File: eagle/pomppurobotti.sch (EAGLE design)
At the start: 23 parts, among them Q1 MOSFET-NCHANNELFQP30N06L

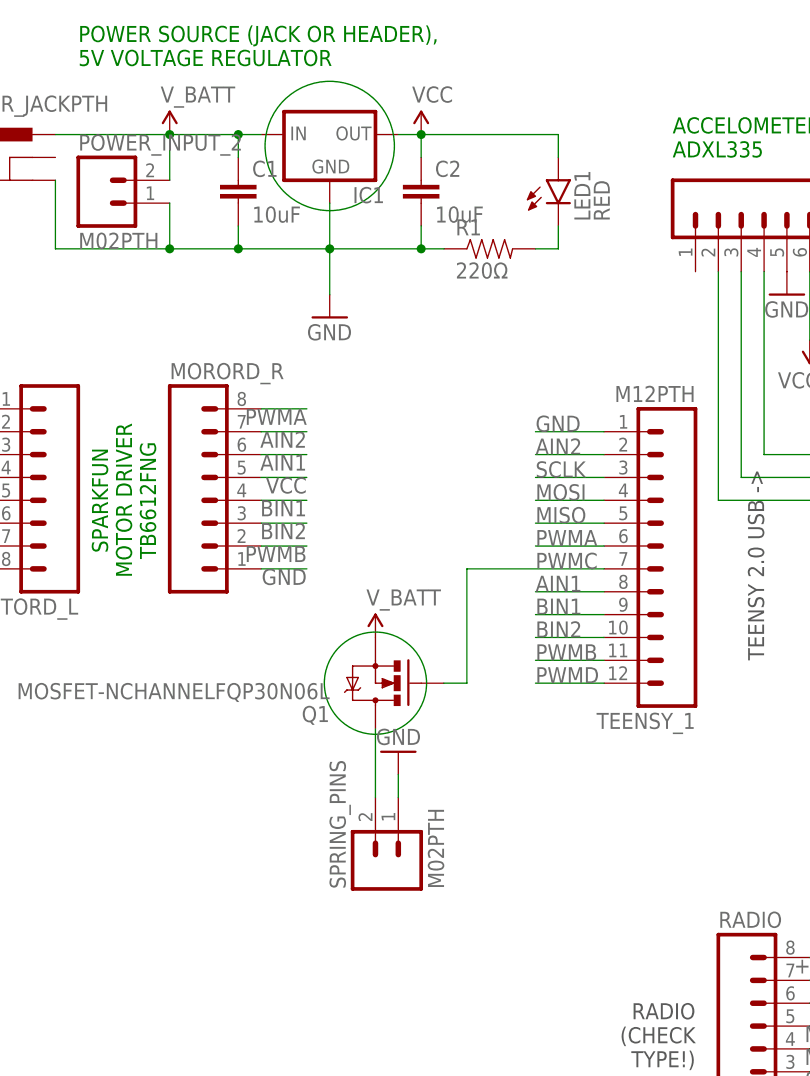
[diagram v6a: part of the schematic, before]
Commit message: Add Arduino tests and modified RF library. Update Eagle schematics.
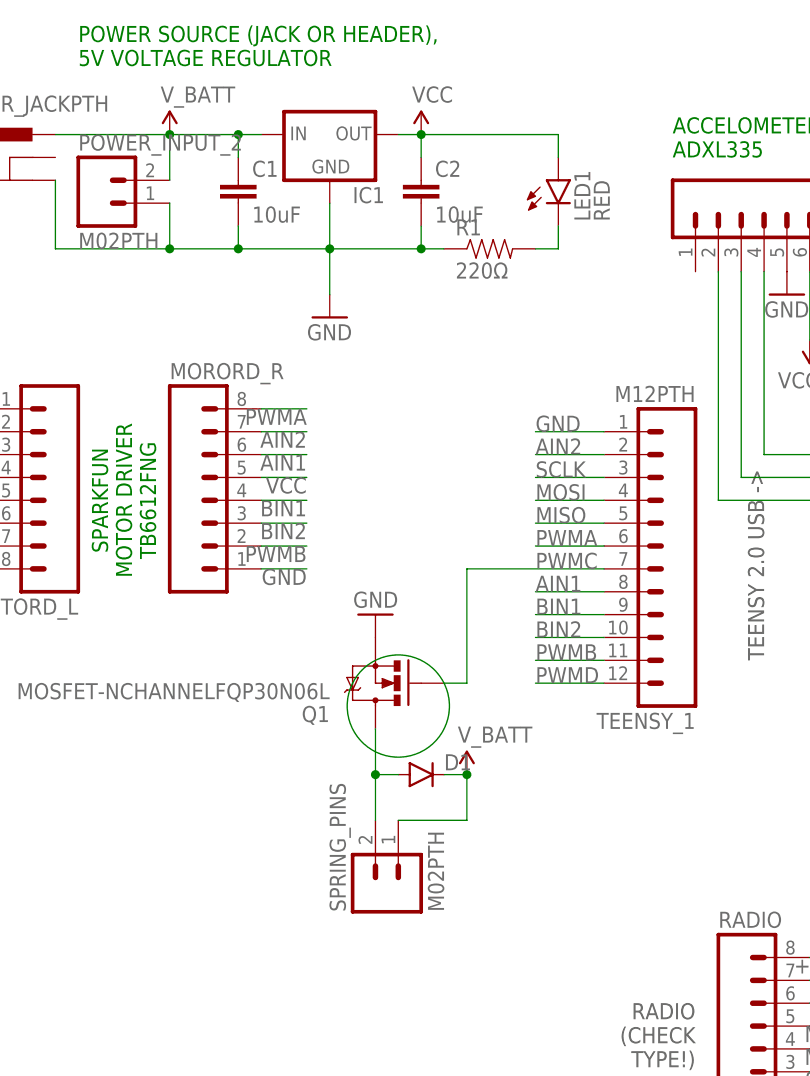
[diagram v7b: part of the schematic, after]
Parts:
- added D1: (no value), SparkFun-DiscreteSemi:DIODEPTH
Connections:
- net GND: now also Q1.S; no longer SPRING_PINS.1
- net N$5: now also D1.A
- net V_BATT: now also D1.C, SPRING_PINS.1; no longer Q1.S
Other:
- moved on the sheet: SPRING_PINS
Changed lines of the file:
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@@
 <layers>
 <layer number="1" name="Top" color="4" fill="1" visible="no" active="no"/>
-<layer number="16" name="Bottom" color="1" fill="1" visible="no" active="no"/>
+<layer number="16" name="Bottom" color="9" fill="1" visible="no" active="no"/>
 <layer number="17" name="Pads" color="2" fill="1" visible="no" active="no"/>
 <layer number="18" name="Vias" color="2" fill="1" visible="no" active="no"/>
@@
 <part name="SUPPLY4" library="SparkFun-Aesthetics" deviceset="V_BATT" device=""/>
 <part name="SUPPLY10" library="SparkFun-Aesthetics" deviceset="V_BATT" device=""/>
+<part name="D1" library="SparkFun-DiscreteSemi" deviceset="DIODE" device="PTH"/>
 </parts>
 <sheets>
@@
 <text x="238.76" y="5.08" size="1.778" layer="91">EXTRA
 PINS</text>
-<circle x="127" y="-5.08" radius="5.6796125" width="0.1524" layer="91"/>
-<circle x="121.92" y="54.61" radius="7.184203125" width="0.1524" layer="91"/>
+<circle x="129.54" y="-7.62" radius="5.6796125" width="0.1524" layer="91"/>
 </plain>
 <instances>
@@
 <instance part="LED2" gate="G$1" x="195.58" y="-17.78"/>
 <instance part="GND2" gate="1" x="195.58" y="-25.4"/>
-<instance part="SPRING_PINS" gate="G$1" x="129.54" y="-25.4" rot="R90"/>
-<instance part="GND3" gate="1" x="129.54" y="-12.7" rot="R180"/>
+<instance part="SPRING_PINS" gate="G$1" x="129.54" y="-27.94" rot="R90"/>
+<instance part="GND3" gate="1" x="127" y="2.54" rot="R180"/>
 <instance part="S1" gate="G$1" x="205.74" y="-2.54" smashed="yes">
 <attribute name="NAME" x="203.2" y="-5.08" size="1.778" layer="95"/>
@@
 <instance part="POWER_INPUT_2" gate="G$1" x="96.52" y="48.26"/>
 <instance part="SUPPLY9" gate="G$1" x="104.14" y="55.88"/>
-<instance part="SUPPLY4" gate="G$1" x="127" y="0"/>
+<instance part="SUPPLY4" gate="G$1" x="137.16" y="-15.24"/>
 <instance part="SUPPLY10" gate="G$1" x="83.82" y="25.4" rot="R90"/>
+<instance part="D1" gate="G$1" x="132.08" y="-15.24"/>
 </instances>
 <busses>
@@
 </segment>
 <segment>
-<pinref part="SPRING_PINS" gate="G$1" pin="1"/>
-<pinref part="GND3" gate="1" pin="GND"/>
-<wire x1="129.54" y1="-17.78" x2="129.54" y2="-15.24" width="0.1524" layer="91"/>
-</segment>
-<segment>
 <pinref part="ACCELOM" gate="G$1" pin="5"/>
 <pinref part="GND4" gate="1" pin="GND"/>
@@
 <pinref part="GND8" gate="1" pin="GND"/>
 <pinref part="RV1" gate="G$1" pin="E"/>
+</segment>
+<segment>
+<pinref part="Q1" gate="G$1" pin="S"/>
+<pinref part="GND3" gate="1" pin="GND"/>
 </segment>
 </net>
@@
 <pinref part="Q1" gate="G$1" pin="D"/>
 <pinref part="SPRING_PINS" gate="G$1" pin="2"/>
-<wire x1="127" y1="-10.16" x2="127" y2="-17.78" width="0.1524" layer="91"/>
+<wire x1="127" y1="-10.16" x2="127" y2="-15.24" width="0.1524" layer="91"/>
+<pinref part="D1" gate="G$1" pin="A"/>
+<wire x1="127" y1="-15.24" x2="127" y2="-20.32" width="0.1524" layer="91"/>
+<wire x1="129.54" y1="-15.24" x2="127" y2="-15.24" width="0.1524" layer="91"/>
+<junction x="127" y="-15.24"/>
 </segment>
 </net>
@@
 </segment>
 <segment>
-<pinref part="Q1" gate="G$1" pin="S"/>
-<pinref part="SUPPLY4" gate="G$1" pin="V_BATT"/>
-</segment>
-<segment>
 <pinref part="MOTORD_L" gate="G$1" pin="1"/>
 <pinref part="SUPPLY10" gate="G$1" pin="V_BATT"/>
 </segment>
-</net>
+<segment>
+<pinref part="SPRING_PINS" gate="G$1" pin="1"/>
+<wire x1="129.54" y1="-20.32" x2="137.16" y2="-20.32" width="0.1524" layer="91"/>
+<wire x1="137.16" y1="-20.32" x2="137.16" y2="-15.24" width="0.1524" layer="91"/>
+<pinref part="SUPPLY4" gate="G$1" pin="V_BATT"/>
+<pinref part="D1" gate="G$1" pin="C"/>
+<wire x1="134.62" y1="-15.24" x2="137.16" y2="-15.24" width="0.1524" layer="91"/>
+<junction x="137.16" y="-15.24"/>
+</segment>
+</net>
